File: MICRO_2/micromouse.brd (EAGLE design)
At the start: 100 x 80 mm, 26 parts

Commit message: Add files via upload
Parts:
- removed C1: (no value), capacitor-wima:C2.5-3
- removed R1, R2, R3, R4, R5: 10k, rcl:0204/5
- removed R10, R6, R7, R8, R9: 330, rcl:0204/5
- removed U$15: VOLTAGE_REGULATOR, VOLTAGE_REGULATOR:VOLTAGE_REGULATOR
- U$1: value TEENSY3.2 -> MOTOR_ENCODER; device teensy_3.2:TEENSY3.2 -> MOTOR_ENCODER:MOTOR_ENCODER
- U$10, U$11, U$12: value IR_EMITTER -> IR_RECIEVER; device IR_EMITTER:IR_EMITTER -> IR_RECIEVER:IR_RECIEVER
- U$13, U$14: value MOTOR_ENCODER -> IR_RECIEVER; device MOTOR_ENCODER:MOTOR_ENCODER -> IR_RECIEVER:IR_RECIEVER
- U$2: value MOTOR_DRIVER -> MOTOR_ENCODER; device motor_driver:MOTOR_DRIVER -> MOTOR_ENCODER:MOTOR_ENCODER
- U$3: value IR_RECIEVER -> TEENSY_3.1-3.2_DIL; device IR_RECIEVER:IR_RECIEVER -> Teensy_3_and_LC_Series_Boards_v1.4:TEENSY_3.0-3.2&LC_DIL
- U$4: value IR_RECIEVER -> MOTOR_DRIVER; device IR_RECIEVER:IR_RECIEVER -> motor_driver:MOTOR_DRIVER
- U$5, U$6, U$7: value IR_RECIEVER -> IR_EMITTER; device IR_RECIEVER:IR_RECIEVER -> IR_EMITTER:IR_EMITTER
- moved U$12 215.9 mm to (-67.3, -86.4)
- moved U$10 211.7 mm to (-67.3, -63.5)
- moved U$14 199.2 mm to (-67.3, -109.2)
- moved U$5 177.3 mm to (-67.3, -6.35)
- moved U$7 164.1 mm to (-67.3, -29.2)
- moved U$4 163.9 mm to (-64.8, 10.2)
- moved U$8 160.8 mm to (-67.3, -40.6)
- moved U$11 152.8 mm to (-67.3, -74.9)
- moved U$9 145.1 mm to (-67.3, -52.1)
- moved U$13 141.3 mm to (-67.3, -97.8)
- moved U$6 112.7 mm to (-67.3, -17.8)
- moved U$2 64.8 mm to (-16.5, 10.2)
- moved U$1 59.6 mm to (-5.08, 10.2)
- moved U$3 53.9 mm to (-39.4, 24.1)
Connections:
- removed net N$1: U$1.2, U$2.M1_ENABLE
- removed net N$10: R6.1, U$1.0
- removed net N$11: R7.1, U$9.1
- removed net N$12: R7.2, U$1.7
- removed net N$13: R8.1, U$10.1
- removed net N$14: R8.2, U$1.8
- removed net N$15: R9.1, U$11.1
- removed net N$16: R9.2, U$1.11
- removed net N$17: R10.1, U$12.1
- removed net N$18: R10.2, U$1.12
- removed net N$19: R1.2, U$1.15, U$4.P$2
- removed net N$2: U$1.3, U$2.M1_FWD_PWN
- removed net N$20: R2.1, U$1.16, U$5.P$2
- removed net N$21: R4.2, U$1.17, U$6.P$2
- removed net N$22: R5.1, U$1.18, U$7.P$2
- removed net N$24: R3.2, U$1.14, U$3.P$2
- removed net N$25: U$13.P$2, U$2.L_M1_1
- removed net N$26: U$1.20, U$14.P$5
- removed net N$27: U$1.13, U$13.P$4
- removed net N$28: U$1.21, U$14.P$4
- removed net N$29: U$1.19, U$13.P$5
- removed net N$3: U$13.P$3, U$2.L_M1_2
- removed net N$30: C1.1, U$1.26, U$13.P$6, U$14.P$6, U$15.P$1, U$2.L_5V, U$2.R_5V
- removed net N$32: U$14.P$2, U$2.R_M2_1
- removed net N$36: U$1.24, U$3.P$1, U$4.P$1, U$5.P$1, U$6.P$1, U$7.P$1
- removed net N$4: U$1.1, U$2.M2_ENABLE
- removed net N$5: U$1.5, U$2.M2_REV_PWM
- removed net N$6: U$14.P$3, U$2.R_M2_2
- removed net N$7: U$1.6, U$2.M2_FWD_PWN
- removed net N$8: U$1.4, U$2.M1_REV_PWN
- removed net N$9: R6.2, U$8.1
- new net 3.3V: U$3.3.3V
- new net AGND: U$3.AGND
- new net VIN: U$3.VIN
- net GND: now also U$3.GND; no longer C1.2, R1.1, R2.2, R3.1, R4.1, R5.2, U$1.GND, U$10.2, U$11.2, U$12.2, U$13.P$1, U$14.P$1, U$15.P$2, U$2.L_GND_1, U$2.L_GND_2, U$2.R_GND_1, U$2.R_GND_2, U$8.2, U$9.2
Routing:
- net GND: track 446.5 -> 0.00 mm, vias 1 -> 0
- net N$36: track 190.8 -> 0.00 mm, vias 8 -> 0
- net N$30: track 153.2 -> 0.00 mm
- net N$29: track 85.3 -> 0.00 mm, vias 1 -> 0
- net N$21: track 76.6 -> 0.00 mm, vias 2 -> 0
- net N$14: track 72.5 -> 0.00 mm, vias 7 -> 0
- net N$24: track 72.3 -> 0.00 mm, vias 7 -> 0
- net N$18: track 67.7 -> 0.00 mm, vias 1 -> 0
- net N$20: track 59.6 -> 0.00 mm, vias 2 -> 0
- net N$2: track 52.3 -> 0.00 mm, vias 4 -> 0
- net N$12: track 51.6 -> 0.00 mm
- net N$28: track 49.8 -> 0.00 mm, vias 4 -> 0
- net N$27: track 49.0 -> 0.00 mm, vias 2 -> 0
- net N$7: track 48.7 -> 0.00 mm, vias 2 -> 0
- net N$19: track 48.6 -> 0.00 mm
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
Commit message: Add files via upload
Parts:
- removed U$13, U$14: IR_RECIEVER, IR_RECIEVER:IR_RECIEVER
- added R1, R3, R5: 330, rcl:0207/10
- added R2, R4: 10K, rcl:0207/10
- added R6: 10k, rcl:0207/10
- U$10: value IR_RECIEVER -> VOLTAGE_REGULATOR; device IR_RECIEVER:IR_RECIEVER -> VOLTAGE_REGULATOR:VOLTAGE_REGULATOR
- U$11: value IR_RECIEVER -> BATTERY_INPUT; device IR_RECIEVER:IR_RECIEVER -> Battery_input:BATTERY_INPUT
- U$5, U$8: value IR_EMITTER -> IR_RECIEVER; device IR_EMITTER:IR_EMITTER -> IR_RECIEVER:IR_RECIEVER
- moved U$1 386.1 mm to (-81.3, -368.3)
- moved U$2 378.9 mm to (1.27, -368.3)
- moved U$4 377.7 mm to (-101.6, -365.8)
- moved U$11 334.8 mm to (-104.1, -407.7)
- moved U$10 330.8 mm to (-102.9, -392.4)
- moved U$7 309.1 mm to (-2.54, -331.5)
- moved U$6 307.9 mm to (-2.54, -318.8)
- moved U$5 299.7 mm to (-64.8, -306.1)
- moved U$9 294.6 mm to (-66.0, -346.7)
- moved U$8 258.8 mm to (-1.27, -290.8)
- moved U$12 202.8 mm to (-1.27, -278.1)
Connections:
- net 3.3V renamed N$5
- removed net GND: U$3.GND
- removed net VIN: U$3.VIN
- new net N$1: U$10.P$3, U$11.VIN
- new net N$10: U$3.13, U$4.M2_ENABLE
- new net N$11: U$1.P$2, U$4.L_M1_1
- new net N$12: U$1.P$3, U$4.L_M1_2
- new net N$13: U$2.P$2, U$4.R_M2_1
- new net N$14: U$2.P$3, U$4.R_M2_2
- new net N$15: U$1.P$4, U$3.10
- new net N$16: U$1.P$5, U$3.11
- new net N$17: U$2.P$5, U$3.8
- new net N$18: U$2.P$4, U$3.9
- new net N$2: U$1.P$1, U$10.P$2, U$11.GND, U$2.P$1, U$3.GND, U$4.L_GND_1, U$4.L_GND_2, U$4.R_GND_1, U$4.R_GND_2
- new net N$3: U$1.P$6, U$10.P$1, U$2.P$6, U$3.VIN, U$4.L_5V, U$4.R_5V
- new net N$4: U$3.12, U$4.M1_ENABLE
- new net N$6: U$3.20/A6, U$4.M1_FWD_PWN
- new net N$7: U$3.21/A7, U$4.M1_REV_PWN
- new net N$8: U$3.22/A8, U$4.M2_REV_PWM
- new net N$9: U$3.23/A9, U$4.M2_FWD_PWN

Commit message: Add files via upload
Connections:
- new net N$19: R1.2, U$3.0
- new net N$20: R1.1, U$9.1
- new net N$21: R6.1, U$3.14/A0, U$8.2
- new net N$22: R3.2, U$3.1
- new net N$23: R3.1, U$6.1
- new net N$24: R4.1, U$12.2, U$3.15/A1
- new net N$25: R5.2, U$3.2
- new net N$26: R5.1, U$7.1
- new net N$28: R2.1, U$3.16/A2, U$5.2
- net N$2: now also R2.2, R4.2, R6.2, U$6.2, U$7.2, U$9.2
- net N$5: now also U$12.1, U$5.1, U$8.1
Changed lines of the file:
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@@
 <contactref element="U$1" pad="P$1"/>
 <contactref element="U$2" pad="P$1"/>
+<contactref element="U$9" pad="2"/>
+<contactref element="U$6" pad="2"/>
+<contactref element="U$7" pad="2"/>
+<contactref element="R6" pad="2"/>
+<contactref element="R4" pad="2"/>
+<contactref element="R2" pad="2"/>
+<wire x1="-57.15" y1="-163.83" x2="-57.15" y2="-191.77" width="0" layer="19" extent="1-1"/>
+<wire x1="-57.15" y1="-135.89" x2="-57.15" y2="-163.83" width="0" layer="19" extent="1-1"/>
+<wire x1="0" y1="-318.77" x2="-57.15" y2="-191.77" width="0" layer="19" extent="1-1"/>
+<wire x1="0" y1="-331.47" x2="0" y2="-318.77" width="0" layer="19" extent="1-1"/>
+<wire x1="0" y1="-364.49" x2="0" y2="-331.47" width="0" layer="19" extent="1-1"/>
+<wire x1="-63.5" y1="-346.71" x2="0" y2="-331.47" width="0" layer="19" extent="1-1"/>
+<wire x1="-82.55" y1="-364.49" x2="-63.5" y2="-346.71" width="0" layer="19" extent="1-1"/>
+<wire x1="-97.79" y1="-367.03" x2="-82.55" y2="-364.49" width="0" layer="19" extent="1-1"/>
+<wire x1="-97.79" y1="-369.57" x2="-97.79" y2="-367.03" width="0" layer="19" extent="1-1"/>
+<wire x1="-105.41" y1="-369.57" x2="-97.79" y2="-369.57" width="0" layer="19" extent="1-1"/>
+<wire x1="-105.41" y1="-367.03" x2="-105.41" y2="-369.57" width="0" layer="19" extent="1-1"/>
+<wire x1="-102.87" y1="-392.43" x2="-105.41" y2="-369.57" width="0" layer="19" extent="1-1"/>
 <wire x1="-102.87" y1="-407.67" x2="-102.87" y2="-392.43" width="0" layer="19" extent="1-1"/>
-<wire x1="-105.41" y1="-369.57" x2="-102.87" y2="-392.43" width="0" layer="19" extent="1-1"/>
-<wire x1="-105.41" y1="-367.03" x2="-105.41" y2="-369.57" width="0" layer="19" extent="1-1"/>
-<wire x1="-97.79" y1="-369.57" x2="-105.41" y2="-369.57" width="0" layer="19" extent="1-1"/>
-<wire x1="-97.79" y1="-367.03" x2="-97.79" y2="-369.57" width="0" layer="19" extent="1-1"/>
-<wire x1="-82.55" y1="-364.49" x2="-97.79" y2="-367.03" width="0" layer="19" extent="1-1"/>
-<wire x1="0" y1="-364.49" x2="-82.55" y2="-364.49" width="0" layer="19" extent="1-1"/>
-<wire x1="-46.99" y1="40.64" x2="-82.55" y2="-364.49" width="0" layer="19" extent="1-1"/>
+<wire x1="-46.99" y1="40.64" x2="-57.15" y2="-135.89" width="0" layer="19" extent="1-1"/>
 </signal>
 <signal name="N$3">
@@
 <signal name="N$5">
 <contactref element="U$3" pad="3.3V"/>
+<contactref element="U$8" pad="1"/>
+<contactref element="U$12" pad="1"/>
+<contactref element="U$5" pad="1"/>
+<wire x1="-2.54" y1="-290.83" x2="-66.04" y2="-306.07" width="0" layer="19" extent="1-1"/>
+<wire x1="-2.54" y1="-278.13" x2="-2.54" y2="-290.83" width="0" layer="19" extent="1-1"/>
+<wire x1="-31.75" y1="35.56" x2="-2.54" y2="-278.13" width="0" layer="19" extent="1-1"/>
 </signal>
 <signal name="N$6">
@@
 <wire x1="-46.99" y1="15.24" x2="0" y2="-372.11" width="0" layer="19" extent="1-1"/>
 </signal>
+<signal name="N$19">
+<contactref element="U$3" pad="0"/>
+<contactref element="R1" pad="2"/>
+<wire x1="-46.99" y1="38.1" x2="-57.15" y2="-121.92" width="0" layer="19" extent="1-1"/>
+</signal>
+<signal name="N$20">
+<contactref element="R1" pad="1"/>
+<contactref element="U$9" pad="1"/>
+<wire x1="-66.04" y1="-346.71" x2="-67.31" y2="-121.92" width="0" layer="19" extent="1-1"/>
+</signal>
+<signal name="N$22">
+<contactref element="U$3" pad="1"/>
+<contactref element="R3" pad="2"/>
+<wire x1="-46.99" y1="35.56" x2="-57.15" y2="-149.86" width="0" layer="19" extent="1-1"/>
+</signal>
+<signal name="N$23">
+<contactref element="R3" pad="1"/>
+<contactref element="U$6" pad="1"/>
+<wire x1="-2.54" y1="-318.77" x2="-67.31" y2="-149.86" width="0" layer="19" extent="1-1"/>
+</signal>
+<signal name="N$25">
+<contactref element="U$3" pad="2"/>
+<contactref element="R5" pad="2"/>
+<wire x1="-46.99" y1="33.02" x2="-57.15" y2="-177.8" width="0" layer="19" extent="1-1"/>
+</signal>
+<signal name="N$26">
+<contactref element="R5" pad="1"/>
+<contactref element="U$7" pad="1"/>
+<wire x1="-2.54" y1="-331.47" x2="-67.31" y2="-177.8" width="0" layer="19" extent="1-1"/>
+</signal>
+<signal name="N$21">
+<contactref element="U$8" pad="2"/>
+<contactref element="R6" pad="1"/>
+<contactref element="U$3" pad="14/A0"/>
+<wire x1="-67.31" y1="-191.77" x2="0" y2="-290.83" width="0" layer="19" extent="1-1"/>
+<wire x1="-31.75" y1="10.16" x2="-67.31" y2="-191.77" width="0" layer="19" extent="1-1"/>
+</signal>
+<signal name="N$24">
+<contactref element="U$12" pad="2"/>
+<contactref element="R4" pad="1"/>
+<contactref element="U$3" pad="15/A1"/>
+<wire x1="0" y1="-278.13" x2="-67.31" y2="-163.83" width="0" layer="19" extent="1-1"/>
+<wire x1="-31.75" y1="12.7" x2="-67.31" y2="-163.83" width="0" layer="19" extent="1-1"/>
+</signal>
+<signal name="N$28">
+<contactref element="U$5" pad="2"/>
+<contactref element="R2" pad="1"/>
+<contactref element="U$3" pad="16/A2"/>
+<wire x1="-31.75" y1="15.24" x2="-67.31" y2="-135.89" width="0" layer="19" extent="1-1"/>
+<wire x1="-63.5" y1="-306.07" x2="-67.31" y2="-135.89" width="0" layer="19" extent="1-1"/>
+</signal>
 </signals>

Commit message: Add files via upload
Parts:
- moved U$11 496.2 mm to (11.4, 74.9), turned to 180 degrees
- moved U$10 477.1 mm to (10.2, 71.1)
- moved U$9 446.3 mm to (83.8, 73.7)
- moved U$1 443.2 mm to (24.1, 62.2), turned to 270 degrees
- moved U$4 429.8 mm to (41.9, 39.4)
- moved U$5 405.9 mm to (78.7, 73.7)
- moved U$2 385.2 mm to (19.1, 16.5), turned to 90 degrees
- moved U$6 381.3 mm to (91.4, 50.8), turned to 270 degrees
- moved U$7 350.5 mm to (86.4, 7.62)
- moved U$12 332.0 mm to (91.4, 40.6), turned to 90 degrees
- moved U$8 309.7 mm to (81.3, 7.62)
- moved R6 243.8 mm to (68.6, 14.0)
- moved R4 238.5 mm to (68.6, 35.6)
- moved R5 237.4 mm to (68.6, 20.3)
- moved R3 236.3 mm to (68.6, 47.0)
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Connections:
- removed net N$2: R2.2, R4.2, R6.2, U$1.P$1, U$10.P$2, U$11.GND, U$2.P$1, U$3.GND, U$4.L_GND_1, U$4.L_GND_2, U$4.R_GND_1, U$4.R_GND_2, U$6.2, U$7.2, U$9.2
- new net GND: R2.2, R4.2, R6.2, U$1.P$1, U$10.P$2, U$11.BAT_GND, U$2.P$1, U$3.GND, U$4.L_GND_1, U$4.L_GND_2, U$4.R_GND_1, U$4.R_GND_2, U$6.2, U$7.2, U$9.2
- net N$1: now also U$11.BAT_7.4V; no longer U$11.VIN

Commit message: added imu component
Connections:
- net N$3 renamed 5V_VCC
- net N$5 renamed 3.3V_VCC
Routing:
- net 3.3V_VCC: track 0.00 -> 225.8 mm, vias 0 -> 2
- net 5V_VCC: track 0.00 -> 160.3 mm
- net GND: track 0.00 -> 124.2 mm
- net N$21: track 0.00 -> 123.3 mm
- net N$22: track 0.00 -> 84.1 mm
- net N$24: track 0.00 -> 76.1 mm
- net N$18: track 0.00 -> 46.8 mm
- net N$13: track 0.00 -> 46.6 mm
- net N$15: track 0.00 -> 45.7 mm
- net N$16: track 0.00 -> 42.3 mm
- net N$17: track 0.00 -> 40.5 mm
- net N$23: track 0.00 -> 29.5 mm
- net N$20: track 0.00 -> 24.4 mm
- net N$28: track 0.00 -> 22.3 mm

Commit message: Add files via upload
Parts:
- added U$13: IMU, IMU:IMU
- moved U$4 5.08 mm to (36.8, 39.4)
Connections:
- net N$10 renamed M2_ENABLE
- net N$6 renamed M1_FWD_PWM
- net N$7 renamed M1_REV_PWM
- net N$8 renamed M2_REV_PWM
- net N$9 renamed M2_FWD_PWM
- removed net N$11: U$1.P$2, U$4.L_M1_1
- removed net N$12: U$1.P$3, U$4.L_M1_2
- removed net N$13: U$2.P$2, U$4.R_M2_1
- removed net N$14: U$2.P$3, U$4.R_M2_2
- removed net N$15: U$1.P$4, U$3.10
- removed net N$16: U$1.P$5, U$3.11
- removed net N$17: U$2.P$5, U$3.8
- removed net N$18: U$2.P$4, U$3.9
- new net M1_L: U$1.M1, U$4.L_M1_1
- new net M1_R: U$2.M1, U$4.R_M2_1
- new net M2_L: U$1.M2, U$4.L_M1_2
- new net M2_R: U$2.M2, U$4.R_M2_2
- new net N$2: U$13.SCL, U$3.19/A5
- new net N$3: U$13.SDA, U$3.18/A4
- new net OUTA_L: U$1.OUTA, U$3.10
- new net OUTA_R: U$2.OUTA, U$3.9
- new net OUTB_L: U$1.OUTB, U$3.11
- new net OUTB_R: U$2.OUTB, U$3.8
- net 3.3V_VCC: now also U$12.REC_ANO, U$5.REC_ANO, U$8.REC_ANO; no longer U$12.1, U$5.1, U$8.1
- net 5V_VCC: now also U$1.VCC, U$13.VIN, U$2.VCC; no longer U$1.P$6, U$2.P$6
- net GND: now also U$1.GND, U$13.GND, U$2.GND, U$6.EMI_CAT, U$7.EMI_CAT, U$9.EMI_CAT; no longer U$1.P$1, U$2.P$1, U$6.2, U$7.2, U$9.2
- net N$20: now also U$9.EMI_ANO; no longer U$9.1
- net N$21: now also U$8.REC_CAT; no longer U$8.2
- net N$23: now also U$6.EMI_ANO; no longer U$6.1
- net N$24: now also U$12.REC_CAT; no longer U$12.2
- net N$26: now also U$7.EMI_ANO; no longer U$7.1
- net N$28: now also U$5.REC_CAT; no longer U$5.2
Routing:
- net 3.3V_VCC: track 225.8 -> 0.00 mm, vias 2 -> 0
- net 5V_VCC: track 160.3 -> 0.00 mm
- net GND: track 124.2 -> 0.00 mm
- net N$21: track 123.3 -> 0.00 mm
- net N$22: track 84.1 -> 0.00 mm
- net N$24: track 76.1 -> 0.00 mm
- net M1_REV_PWM: track 0.00 -> 64.4 mm
- net N$18: track 46.8 -> 0.00 mm
- net N$13: track 46.6 -> 0.00 mm
- net N$15: track 45.7 -> 0.00 mm
- net N$16: track 42.3 -> 0.00 mm
- net N$17: track 40.5 -> 0.00 mm
- net M2_REV_PWM: track 0.00 -> 38.2 mm
- net N$4: track 0.00 -> 35.7 mm
- net N$23: track 29.5 -> 0.00 mm
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
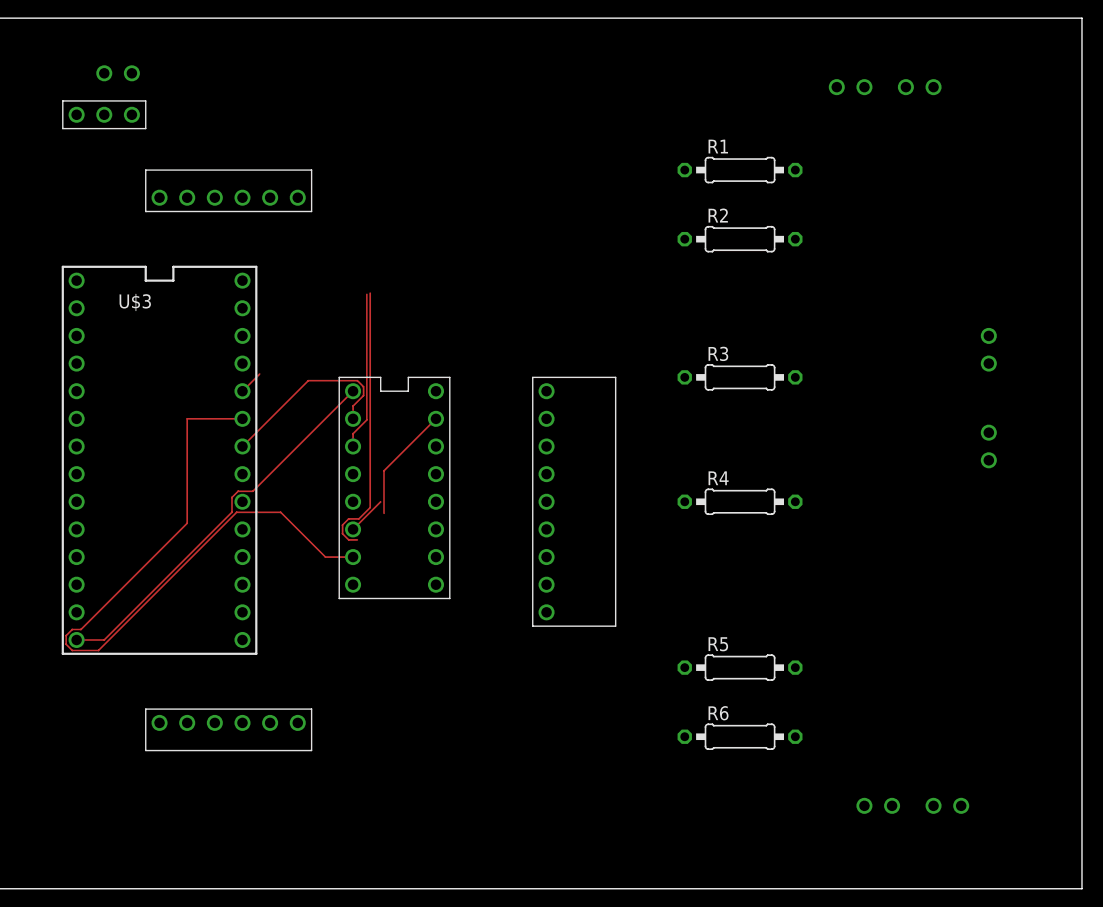
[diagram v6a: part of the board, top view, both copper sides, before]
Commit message: added 2 extra ir pairs
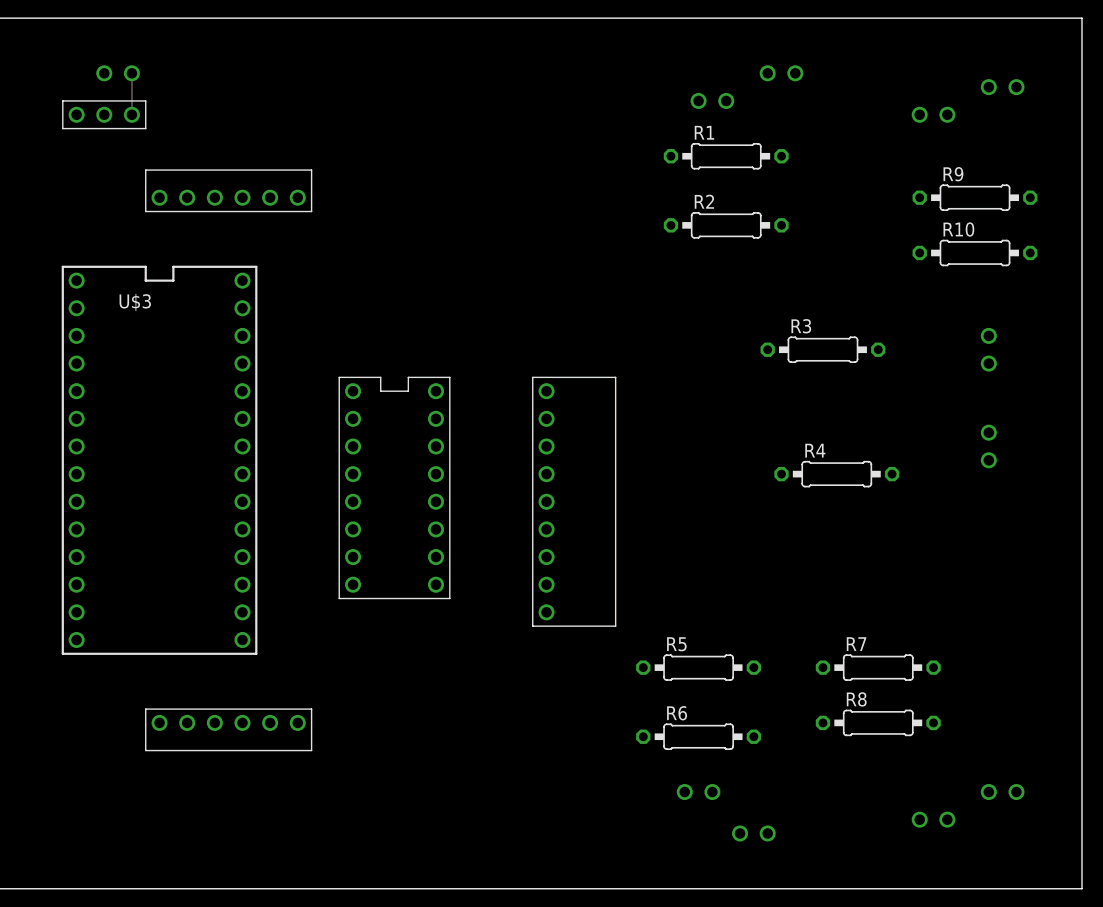
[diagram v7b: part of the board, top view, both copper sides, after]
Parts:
- added R10, R8: 10K, rcl:0207/10
- added R7, R9: 330, rcl:0207/10
- added U$14, U$16: IR_EMITTER, IR_EMITTER:IR_EMITTER
- added U$15, U$17: IR_RECIEVER, IR_RECIEVER:IR_RECIEVER
- moved U$7 18.0 mm to (68.6, 5.08)
- moved U$8 16.6 mm to (64.8, 8.89)
- moved U$9 12.8 mm to (71.1, 74.9)
- moved U$5 12.8 mm to (66.0, 72.4)
- moved R4 9.25 mm to (77.5, 38.1)
- moved R3 8.03 mm to (76.2, 49.5)
- moved R5 3.81 mm to (64.8, 20.3)
- moved R6 3.81 mm to (64.8, 14.0)
- moved R2 1.80 mm to (67.3, 61.0)
- moved R1 1.80 mm to (67.3, 67.3)
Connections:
- removed net M2_REV_PWM: U$3.22/A8, U$4.M2_REV_PWM
- new net N$10: R9.1, U$16.EMI_ANO
- new net N$12: R10.1, U$17.REC_CAT, U$3.23/A9
- new net N$5: U$3.5, U$4.M2_REV_PWM
- new net N$6: R7.2, U$3.3
- new net N$7: R7.1, U$14.EMI_ANO
- new net N$8: R8.1, U$15.REC_CAT, U$3.22/A8
- new net N$9: R9.2, U$3.4
- net 3.3V_VCC: now also U$15.REC_ANO, U$17.REC_ANO
- net 5V_VCC: now also U$10.VOUT; no longer U$10.P$1
- net GND: now also R10.2, R8.2, U$10.GND, U$14.EMI_CAT, U$16.EMI_CAT; no longer U$10.P$2
- net M2_FWD_PWM: now also U$3.6; no longer U$3.23/A9
- net N$1: now also U$10.VIN; no longer U$10.P$3
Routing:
- net M1_REV_PWM: track 64.4 -> 0.00 mm
- net M2_REV_PWM: track 38.2 -> 0.00 mm
- net N$4: track 35.7 -> 0.00 mm
- net M1_FWD_PWM: track 17.2 -> 0.00 mm
- net M1_L: track 14.5 -> 0.00 mm
- net N$1: track 0.00 -> 3.81 mm
- net M2_L: track 3.59 -> 0.00 mm
